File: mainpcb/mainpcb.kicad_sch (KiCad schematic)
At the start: 9 parts, among them J1 Raspberry_Pi_2_3, J10 Conn_02x02_Top_Bottom, J11 Conn_02x02_Top_Bottom, J3 8P8C_Shielded, J8 8P8C_Shielded, J9 Screw_Terminal_01x09, U4 TXB0108PW, U5 TCA9517ADGK

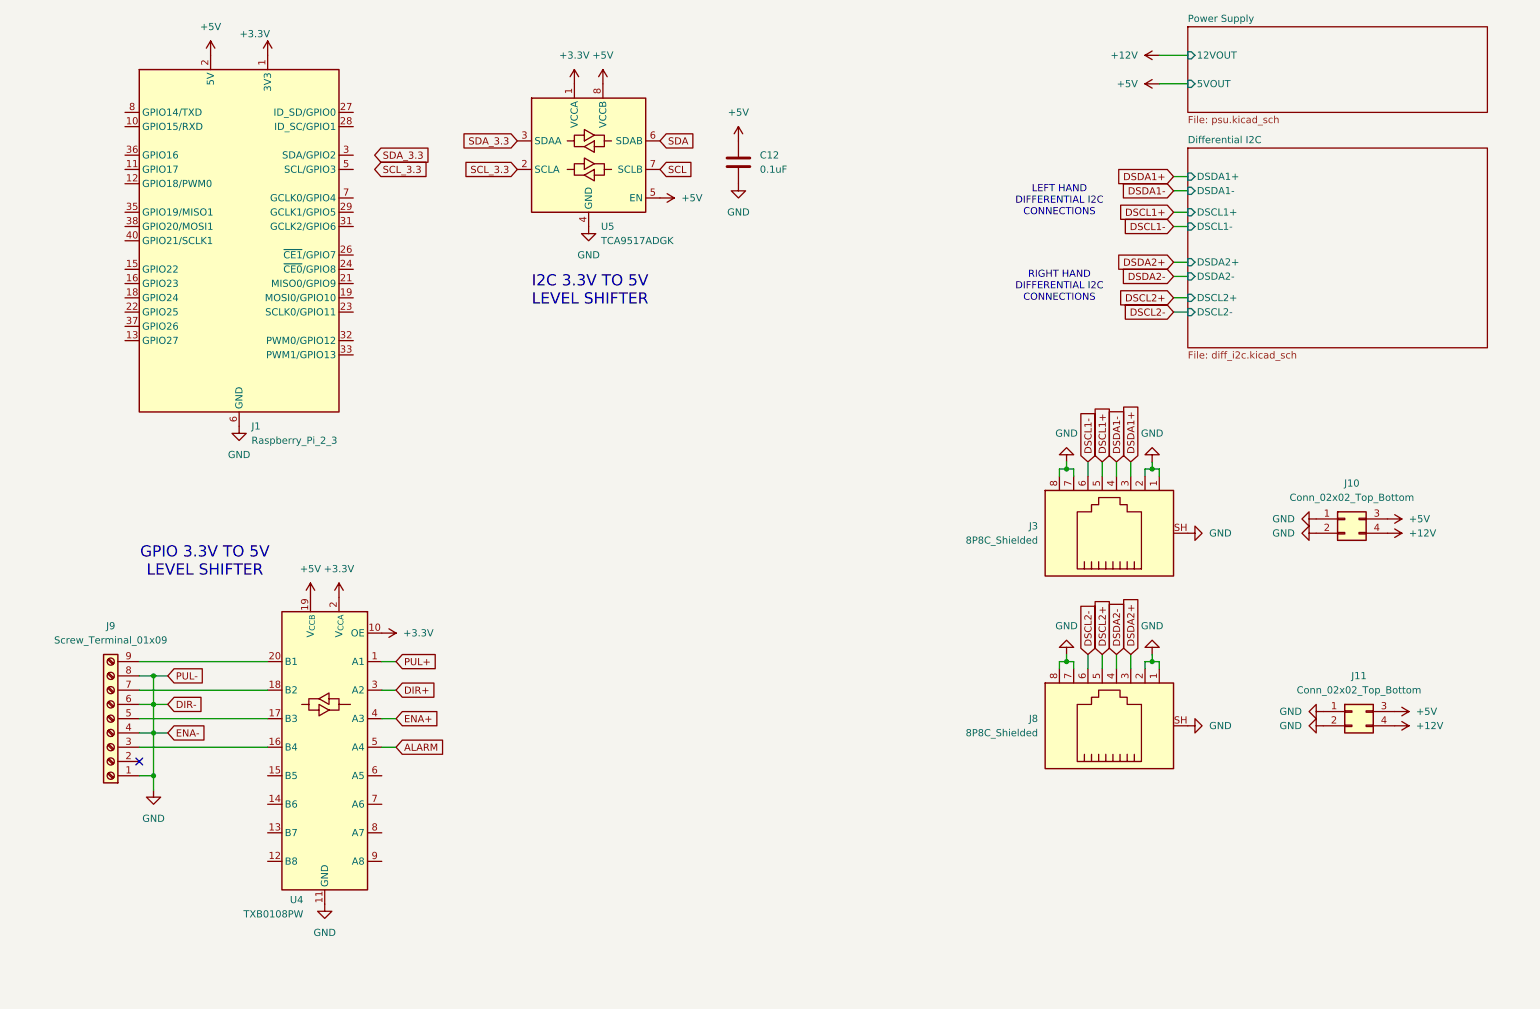
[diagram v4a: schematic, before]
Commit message: Added current and voltage sensing on control board
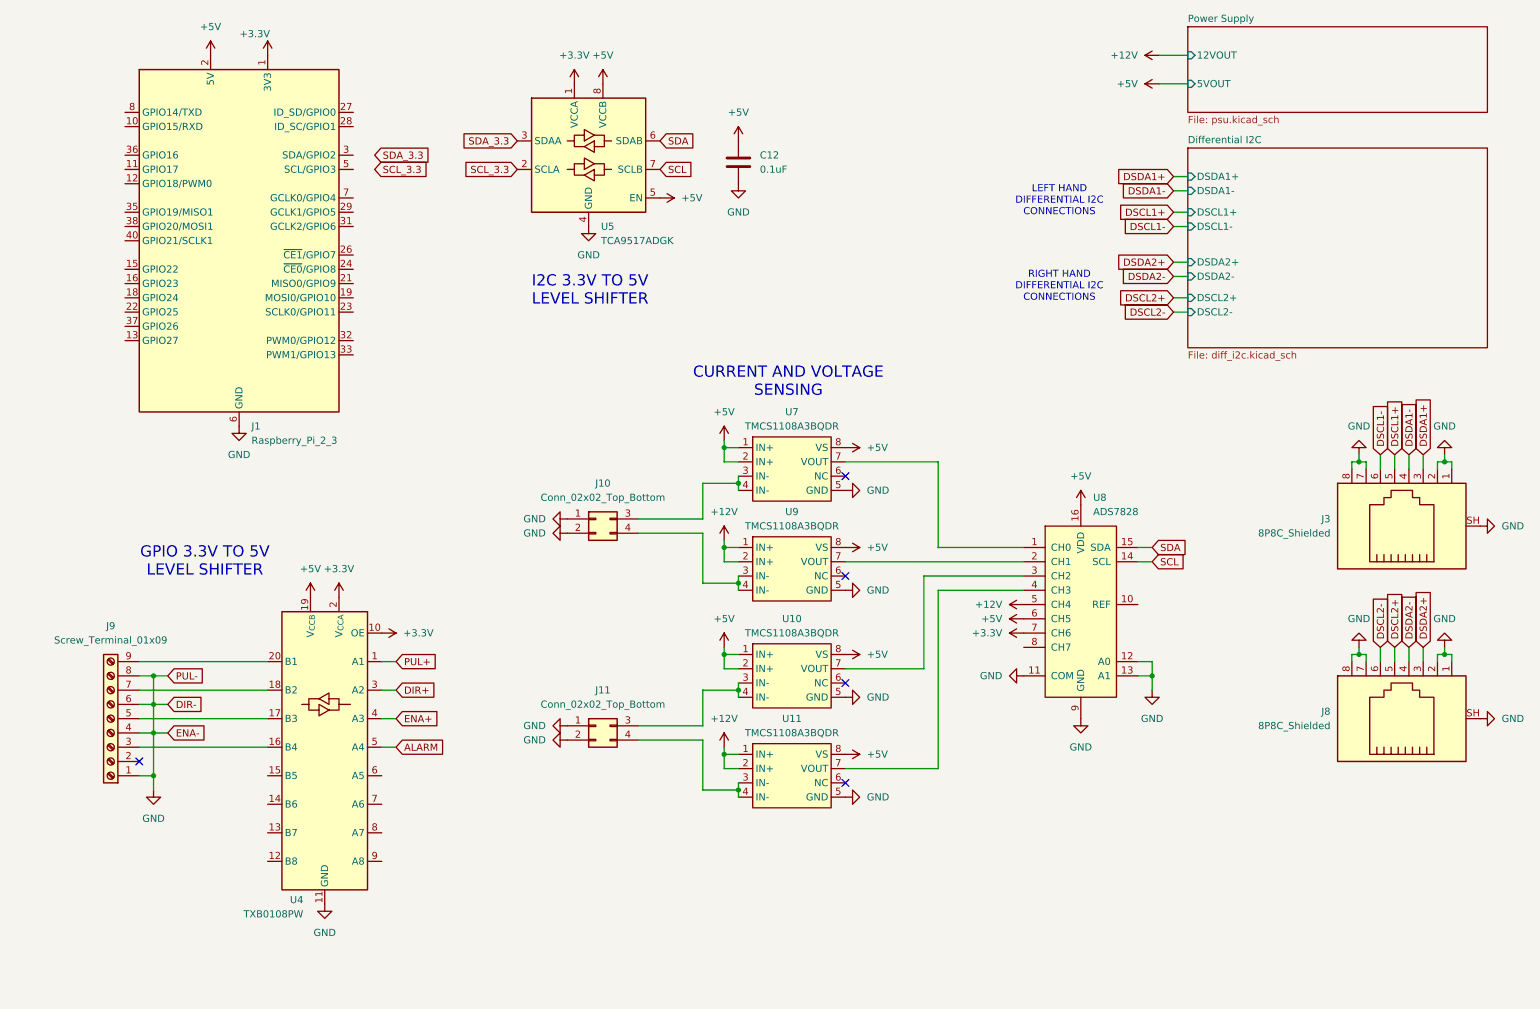
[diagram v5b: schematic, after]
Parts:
- added U10, U11, U7, U9: TMCS1108A3BQDR, Package_SO:SOIC-8-N7_3.9x4.9mm_P1.27mm, symbol bh_symbol_library:TMCS1108A3BQDR
- added U8: ADS7828, Package_SO:TSSOP-16_4.4x5mm_P0.65mm, symbol Analog_ADC:ADS7828
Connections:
- net +12V: now also U11.1 (IN+), U11.2 (IN+), U8.5 (CH4), U9.1 (IN+), U9.2 (IN+); no longer J10.4 (Pin_4), J11.4 (Pin_4)
- net +3.3V: now also U8.7 (CH6)
- net +5V: now also U10.1 (IN+), U10.2 (IN+), U10.8 (VS), U11.8 (VS), U7.1 (IN+), U7.2 (IN+), U7.8 (VS), U8.16 (VDD), U8.6 (CH5), U9.8 (VS); no longer J10.3 (Pin_3), J11.3 (Pin_3)
- net GND: now also U10.5 (GND), U11.5 (GND), U7.5 (GND), U8.11 (COM), U8.12 (A0), U8.13 (A1), U8.9 (GND), U9.5 (GND)
- net SCL: now also U8.14 (SCL)
- net SDA: now also U8.15 (SDA)
- new net: U7.7 (VOUT), U8.1 (CH0)
- new net: U8.2 (CH1), U9.7 (VOUT)
- new net: U10.7 (VOUT), U8.3 (CH2)
- new net: U11.7 (VOUT), U8.4 (CH3)
- new net: J10.3 (Pin_3), U7.3 (IN-), U7.4 (IN-)
- new net: J10.4 (Pin_4), U9.3 (IN-), U9.4 (IN-)
- new net: J11.3 (Pin_3), U10.3 (IN-), U10.4 (IN-)
- new net: J11.4 (Pin_4), U11.3 (IN-), U11.4 (IN-)
- no-connect marks 1 -> 5
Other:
- note added: "CURRENT AND VOLTAGE SENSING"
- moved on the sheet: J10, J11, J3, J8

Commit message: Added limit switches to hand and readme
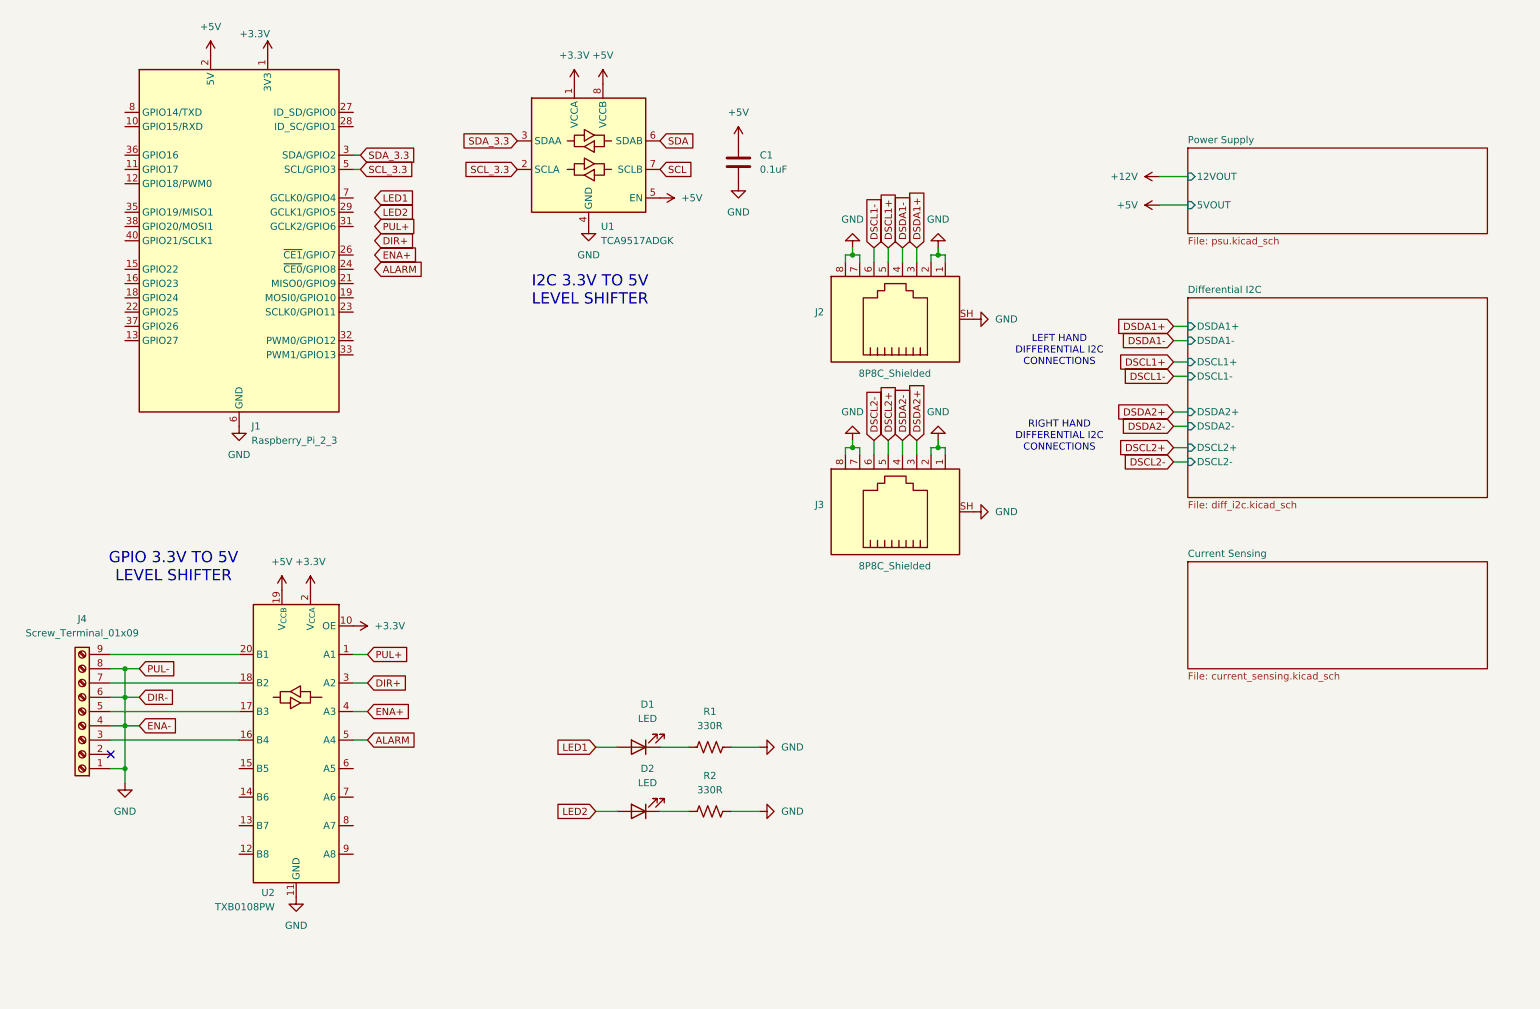
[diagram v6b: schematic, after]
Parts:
- removed J10, J11: Conn_02x02_Top_Bottom, Connector_Molex:Molex_Mini-Fit_Jr_5569-04A2_2x02_P4.20mm_Horizontal, symbol Connector_Generic:Conn_02x02_Top_Bottom
- removed U10, U11, U7, U9: TMCS1108A3BQDR, Package_SO:SOIC-8-N7_3.9x4.9mm_P1.27mm, symbol bh_symbol_library:TMCS1108A3BQDR
- removed U8: ADS7828, Package_SO:TSSOP-16_4.4x5mm_P0.65mm, symbol Analog_ADC:ADS7828
- added D1, D2: LED, LED_THT:LED_D5.0mm_Clear, symbol Device:LED
- added R1, R2: 330R, Resistor_THT:R_Axial_DIN0207_L6.3mm_D2.5mm_P10.16mm_Horizontal, symbol Device:R_US
- C1: renamed from C12; footprint Capacitor_THT:C_Disc_D8.0mm_W2.5mm_P5.00mm -> Capacitor_THT:C_Rect_L4.6mm_W2.0mm_P2.50mm_MKS02_FKP02
- J2: renamed from J3; footprint Connector_RJ:RJ45_Amphenol_RJHSE5380 -> Connector_RJ:RJ45_Amphenol_54602-x08_Horizontal
- J3: renamed from J8; footprint Connector_RJ:RJ45_Amphenol_RJHSE5380 -> Connector_RJ:RJ45_Amphenol_54602-x08_Horizontal
- renumbered J9 to J4, U5 to U1, U4 to U2
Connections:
- net GND: now also R1.2, R2.2
- net SCL_3.3: now also J1.5 (SCL/GPIO3)
- net SDA_3.3: now also J1.3 (SDA/GPIO2)
- new net: D1.1 (K), R1.1
- new net: D2.1 (K), R2.1
- new net LED1: D1.2 (A)
- new net LED2: D2.2 (A)
- no-connect marks 5 -> 1
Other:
- added sheet Current Sensing (current_sensing.kicad_sch)
- note removed: "CURRENT AND VOLTAGE SENSING"
- moved on the sheet: J2, J3, J4, U2

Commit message: Added screw terminals etc for both stepper drivers
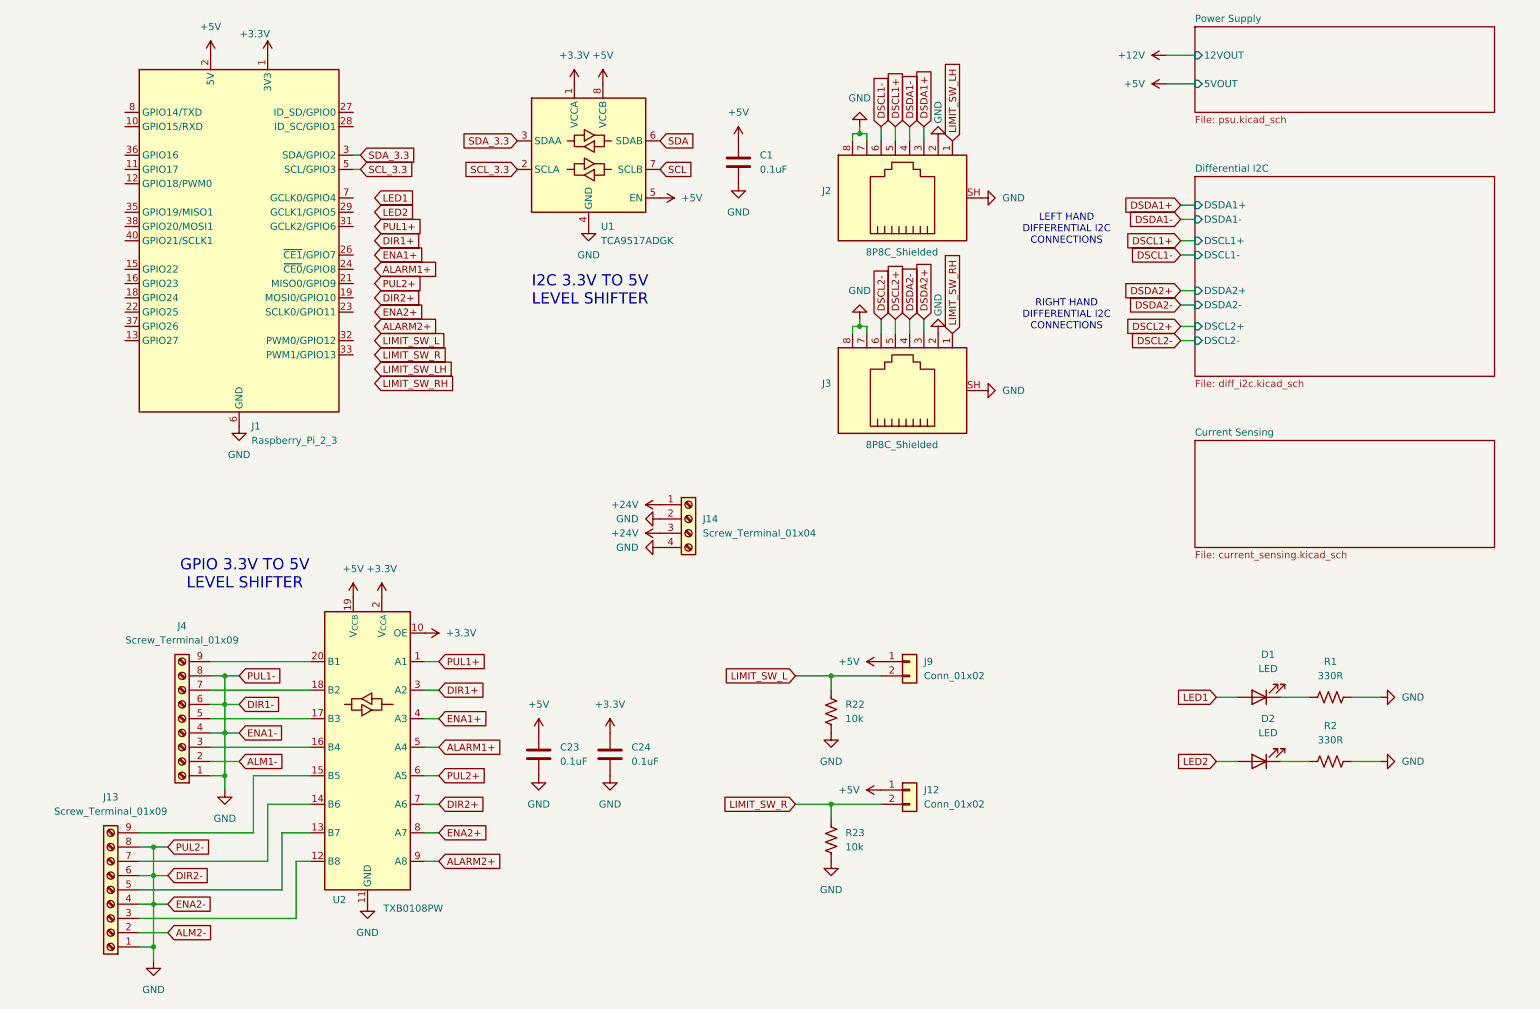
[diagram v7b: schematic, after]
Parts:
- added C23, C24: 0.1uF, Capacitor_THT:C_Rect_L4.6mm_W2.0mm_P2.50mm_MKS02_FKP02, symbol Device:C
- added J12, J9: Conn_01x02, Connector_JST:JST_XH_S2B-XH-A_1x02_P2.50mm_Horizontal, symbol Connector_Generic:Conn_01x02
- added J13: Screw_Terminal_01x09, TerminalBlock_Phoenix:TerminalBlock_Phoenix_PT-1,5-9-5.0-H_1x09_P5.00mm_Horizontal, symbol Connector:Screw_Terminal_01x09
- added J14: Screw_Terminal_01x04, TerminalBlock_Phoenix:TerminalBlock_Phoenix_PT-1,5-4-5.0-H_1x04_P5.00mm_Horizontal, symbol Connector:Screw_Terminal_01x04
- added R22, R23: 10k, Resistor_THT:R_Axial_DIN0207_L6.3mm_D2.5mm_P10.16mm_Horizontal, symbol Device:R_US
- J4: footprint (none) -> TerminalBlock_Phoenix:TerminalBlock_Phoenix_PT-1,5-9-5.0-H_1x09_P5.00mm_Horizontal; Digikey (none) -> https://www.digikey.ca/en/products/detail/phoenix-contact/1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
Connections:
- net +3.3V: now also C24.1
- net +5V: now also C23.1, J12.1 (Pin_1), J9.1 (Pin_1)
- net GND: now also C23.2, C24.2, J13.1 (Pin_1), J13.4 (Pin_4), J13.6 (Pin_6), J13.8 (Pin_8), J14.2 (Pin_2), J14.4 (Pin_4), R22.1, R23.1; no longer J2.1, J3.1
- net at U2.12 (B8): now also J13.3 (Pin_3)
- net at U2.13 (B7): now also J13.5 (Pin_5)
- net at U2.14 (B6): now also J13.7 (Pin_7)
- net at U2.15 (B5): now also J13.9 (Pin_9)
- net PUL2+: now reaches U2.6 (A5)
- net DIR2+: now reaches U2.7 (A6)
- net ENA2+: now reaches U2.8 (A7)
- net ALARM2+: now reaches U2.9 (A8)
- net ALM1-: now reaches J4.2 (Pin_2)
- net ALARM renamed ALARM1+
- net DIR+ renamed DIR1+
- net ENA+ renamed ENA1+
- net PUL+ renamed PUL1+
- new net +24V: J14.1 (Pin_1), J14.3 (Pin_3)
- new net ALM2-: J13.2 (Pin_2)
- new net LIMIT_SW_L: J9.2 (Pin_2), R22.2
- new net LIMIT_SW_LH: J2.1
- new net LIMIT_SW_R: J12.2 (Pin_2), R23.2
- new net LIMIT_SW_RH: J3.1
- no-connect marks 1 -> 0
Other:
- moved on the sheet: D1, D2, J2, J3, J4, R1, R2, U2

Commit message: Started layout of control board
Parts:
- removed J12, J9: Conn_01x02, Connector_JST:JST_XH_S2B-XH-A_1x02_P2.50mm_Horizontal, symbol Connector_Generic:Conn_01x02
- removed J14: Screw_Terminal_01x04, TerminalBlock_Phoenix:TerminalBlock_Phoenix_PT-1,5-4-5.0-H_1x04_P5.00mm_Horizontal, symbol Connector:Screw_Terminal_01x04
- removed R22, R23: 10k, Resistor_THT:R_Axial_DIN0207_L6.3mm_D2.5mm_P10.16mm_Horizontal, symbol Device:R_US
- added J15, J9: Screw_Terminal_01x02, TerminalBlock_Phoenix:TerminalBlock_Phoenix_PT-1,5-2-5.0-H_1x02_P5.00mm_Horizontal, symbol Connector:Screw_Terminal_01x02
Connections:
- net +24V: now also J15.1 (Pin_1), J9.1 (Pin_1)
- net GND: now also J15.2 (Pin_2), J9.2 (Pin_2); no longer J2.8, J3.8
- net ALM1-: no longer names the net of J4.2 (Pin_2)
- net ALM2-: no longer names the net of J13.2 (Pin_2)
- net LIMIT_SW_LH renamed LIMIT_SW_LL
- net LIMIT_SW_RH renamed LIMIT_SW_RL
- new net LIMIT_SW_LR: J2.8
- new net LIMIT_SW_RR: J3.8
